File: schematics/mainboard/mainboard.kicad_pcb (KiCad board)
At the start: 2 copper layers, 166.4 x 91.4 mm, 31 parts, among them J1 ICSP, J2 USB_B_Micro, J3 DEALON DC-S050-200, J4 PWR_SELECT, J5 JOY1, J6 JOY2, J7 Throttle, U1 ATmega2560-16A, U2 FT232RL, U3 USBLC6-2P6, U4 AIP78M05, U5 L9110, Y1 16Mhz

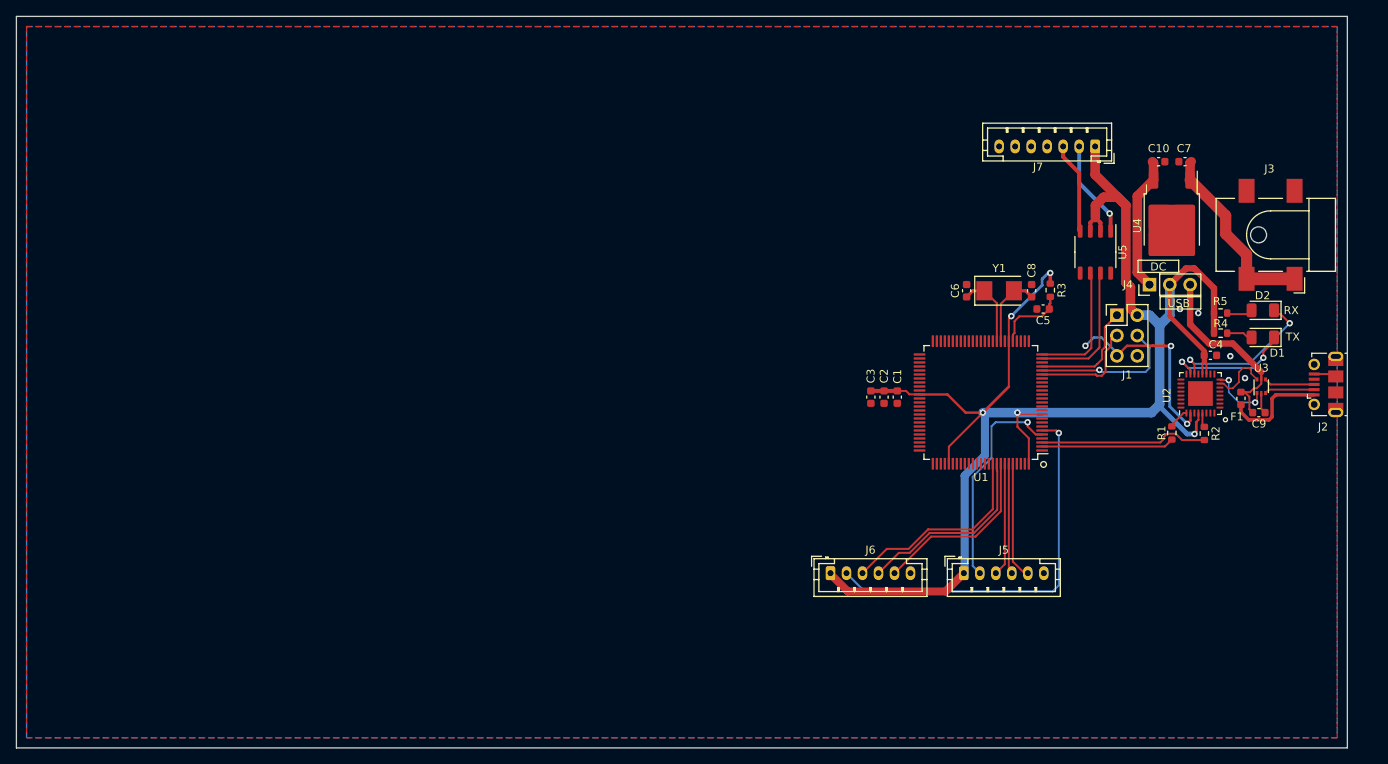
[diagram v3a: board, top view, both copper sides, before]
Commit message: SCH: mainboard=> DGAUGES header
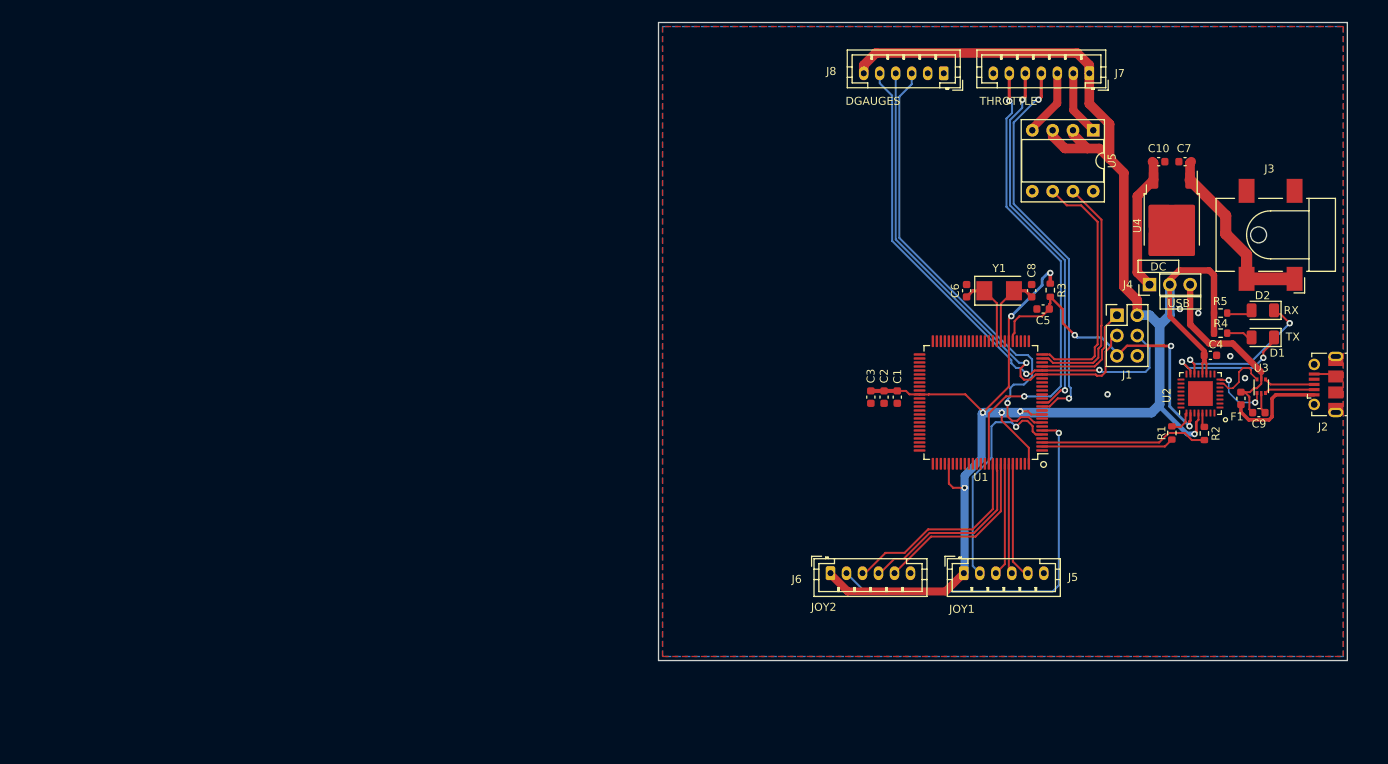
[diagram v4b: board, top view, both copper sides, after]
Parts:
- added J8: DGAUGES, Connector_JST:JST_PH_B6B-PH-K_1x06_P2.00mm_Vertical, F.Cu at (154.0, 28.7)
- U5: footprint Package_SO:SOP-8_3.9x4.9mm_P1.27mm -> Package_DIP:DIP-8_W7.62mm_Socket
- moved U5 15.2 mm to (172.7, 35.8)
- moved J7 9.17 mm to (172.2, 28.7)
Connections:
- U1 pad 8: unconnected-(U1-PE6-Pad8) -> Net-(J8-Pin_3)
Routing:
- net Net-(J7-Pin_6): track 0.00 -> 59.1 mm, vias 0 -> 2
- net Net-(J8-Pin_3): track 0.00 -> 58.3 mm, vias 0 -> 1
- net Net-(J7-Pin_4): track 0.00 -> 49.0 mm, vias 0 -> 2
- net /SCK: track 13.8 -> 62.4 mm, vias 0 -> 1
- net /MOSI: track 18.4 -> 66.1 mm, vias 1 -> 2
- net Net-(J7-Pin_5): track 0.00 -> 46.7 mm, vias 0 -> 2
- net +5V: track 207.2 -> 248.0 mm, vias 5 -> 7
- net /THROTTLE_DOWN: track 15.9 -> 31.1 mm
- net /THROTTLE_UP: track 17.1 -> 30.0 mm
- net /RESET: track 34.2 -> 41.9 mm
- net Net-(J7-Pin_2): track 12.2 -> 8.16 mm, vias 1 -> 0
- net Net-(J7-Pin_3): track 11.5 -> 8.42 mm
- net Net-(U2-TXD): track 2.43 -> 3.24 mm
- net Net-(J5-Pin_2): track 27.2 -> 27.9 mm
- net GND: vias 4 -> 5
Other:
- board size 166.4 x 91.4 mm -> 86.1 x 79.8 mm
- board text added: "DGAUGES"
- board text added: "JOY1"
- board text added: "JOY2"
- board text added: "THROTTLE"

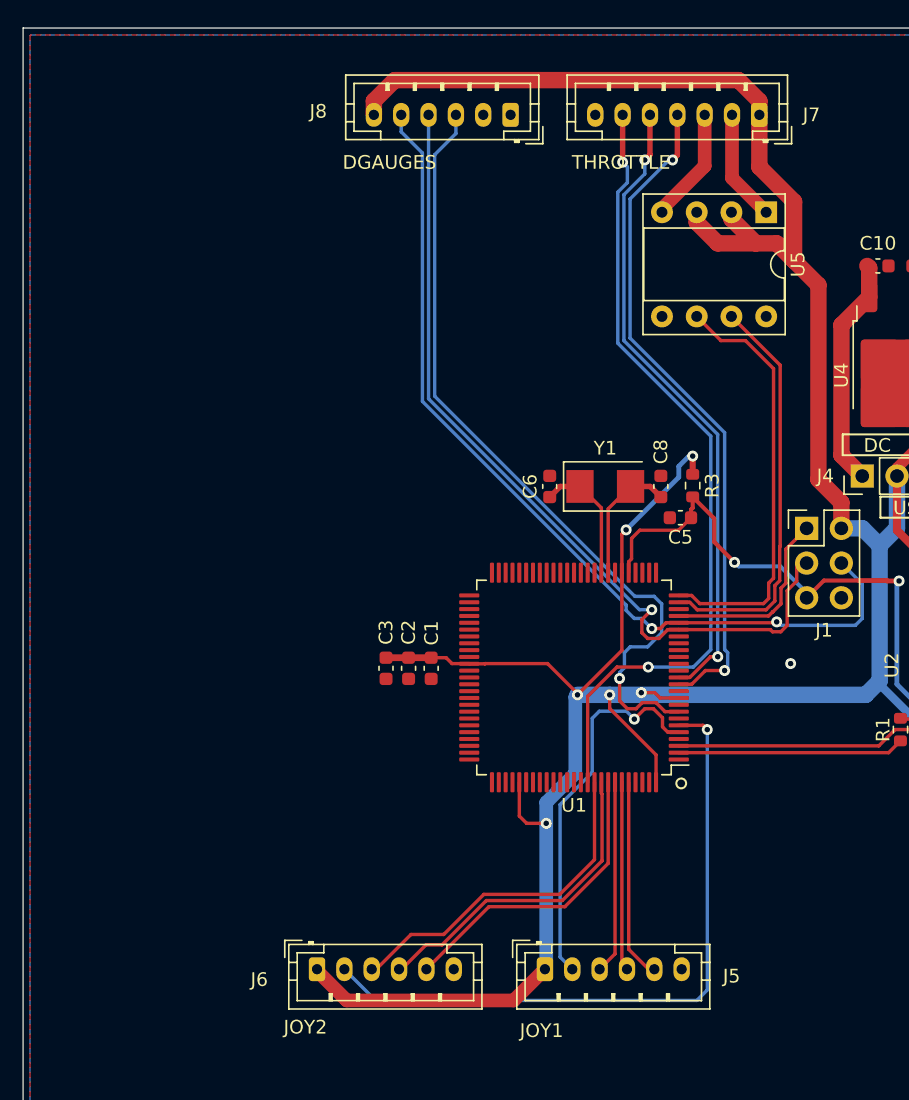
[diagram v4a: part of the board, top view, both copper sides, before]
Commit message: Mainboard: tweak pins, routed lcd connector
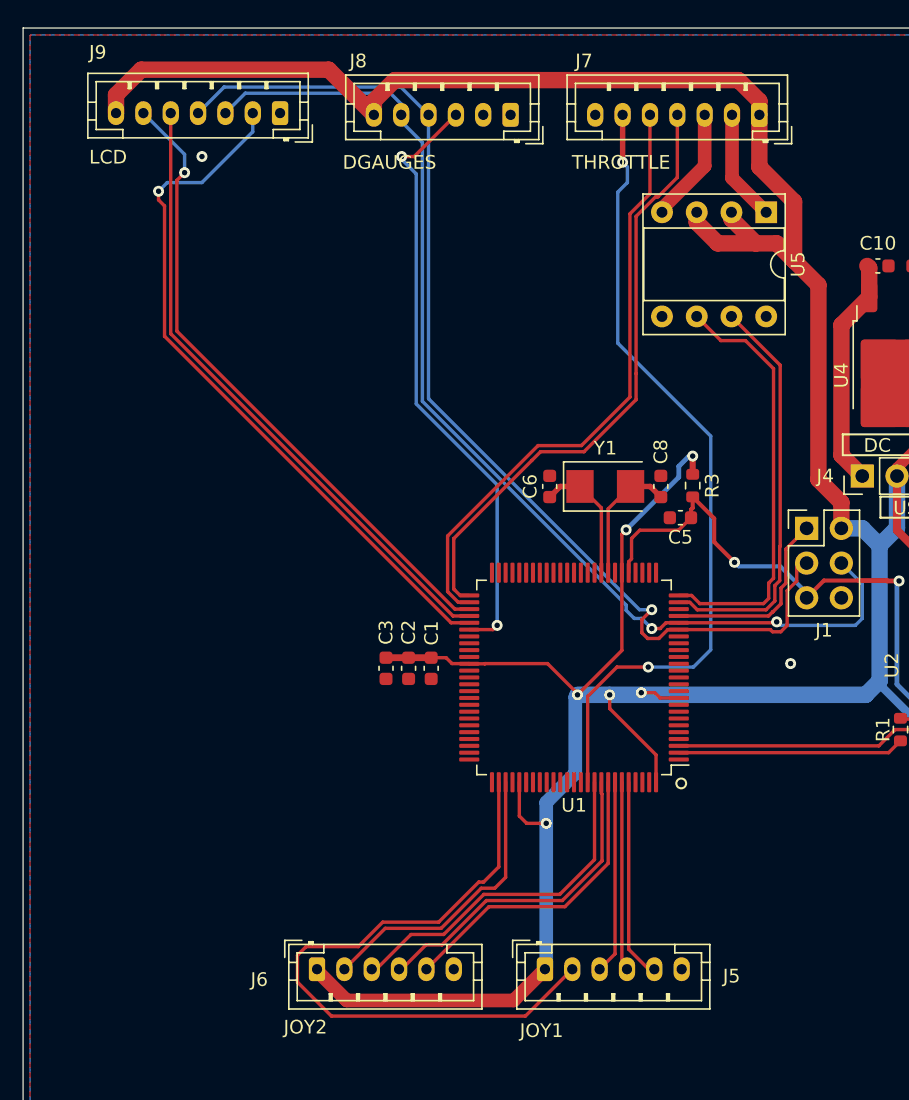
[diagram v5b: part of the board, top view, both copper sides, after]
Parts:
- added J9: LCD, Connector_JST:JST_PH_B7B-PH-K_1x07_P2.00mm_Vertical, F.Cu at (137.2, 28.6)
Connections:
- J5 pad 2: Net-(J5-Pin_2) -> /JOY1_PB
- J6 pad 2: Net-(J6-Pin_2) -> /JOY2_PB
- J8 pad 3: Net-(J8-Pin_3) -> /DG_LATCH
- U1 pad 12: Net-(J7-Pin_4) -> unconnected-(U1-PH0-Pad12)
- U1 pad 13: Net-(J7-Pin_5) -> unconnected-(U1-PH1-Pad13)
- U1 pad 5: Net-(J5-Pin_2) -> unconnected-(U1-PE3-Pad5)
- U1 pad 51: unconnected-(U1-PG0-Pad51) -> Net-(J7-Pin_4)
- U1 pad 52: unconnected-(U1-PG1-Pad52) -> Net-(J7-Pin_5)
- U1 pad 53: unconnected-(U1-PC0-Pad53) -> Net-(J9-Pin_6)
- U1 pad 54: unconnected-(U1-PC1-Pad54) -> Net-(J9-Pin_5)
- U1 pad 55: unconnected-(U1-PC2-Pad55) -> Net-(J9-Pin_2)
- U1 pad 56: unconnected-(U1-PC3-Pad56) -> /DG_LATCH
- U1 pad 6: Net-(J6-Pin_2) -> unconnected-(U1-PE4-Pad6)
- U1 pad 77: unconnected-(U1-PA1-Pad77) -> /JOY1_PB
- U1 pad 78: unconnected-(U1-PA0-Pad78) -> /JOY2_PB
- U1 pad 8: Net-(J8-Pin_3) -> unconnected-(U1-PE6-Pad8)
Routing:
- net Net-(J8-Pin_3): track 58.3 -> 0.00 mm, vias 1 -> 0
- net Net-(J9-Pin_2): track 0.00 -> 51.8 mm, vias 0 -> 1
- net Net-(J6-Pin_2): track 49.1 -> 0.00 mm, vias 1 -> 0
- net /JOY1_PB: track 0.00 -> 48.1 mm
- net Net-(J9-Pin_6): track 0.00 -> 47.2 mm, vias 0 -> 1
- net Net-(J9-Pin_5): track 0.00 -> 46.5 mm
- net /DG_LATCH: track 0.00 -> 44.6 mm, vias 0 -> 2
- net Net-(J5-Pin_2): track 27.9 -> 0.00 mm, vias 1 -> 0
- net +5V: track 248.0 -> 270.4 mm
- net /JOY2_PB: track 0.00 -> 21.5 mm
- net /SCK: track 62.4 -> 80.8 mm
- net /MOSI: track 66.1 -> 80.7 mm
- net Net-(J7-Pin_4): track 49.0 -> 44.7 mm, vias 2 -> 0
- net Net-(J7-Pin_5): track 46.7 -> 44.8 mm, vias 2 -> 0
- net GND: vias 5 -> 6
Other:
- board text added: "LCD"

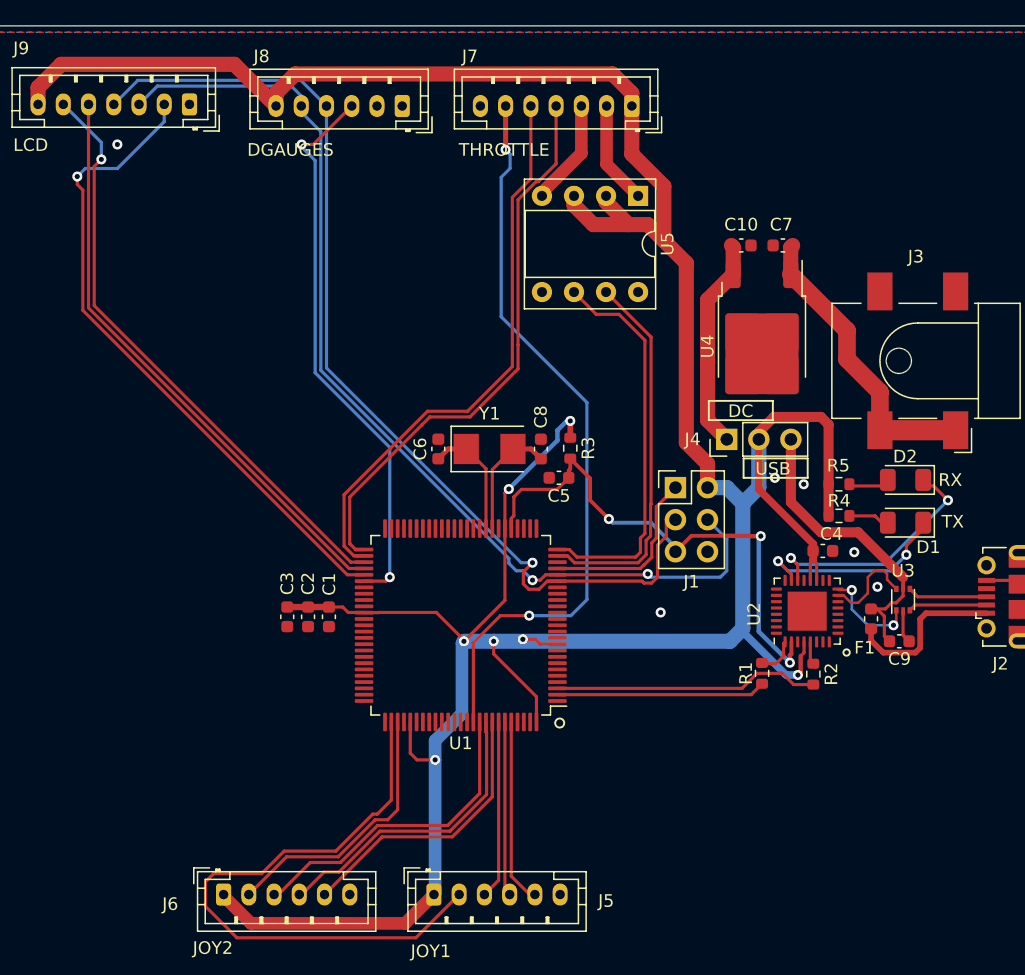
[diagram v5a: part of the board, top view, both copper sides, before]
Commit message: SCH: mainboard missing cap & gnd connections on ft232
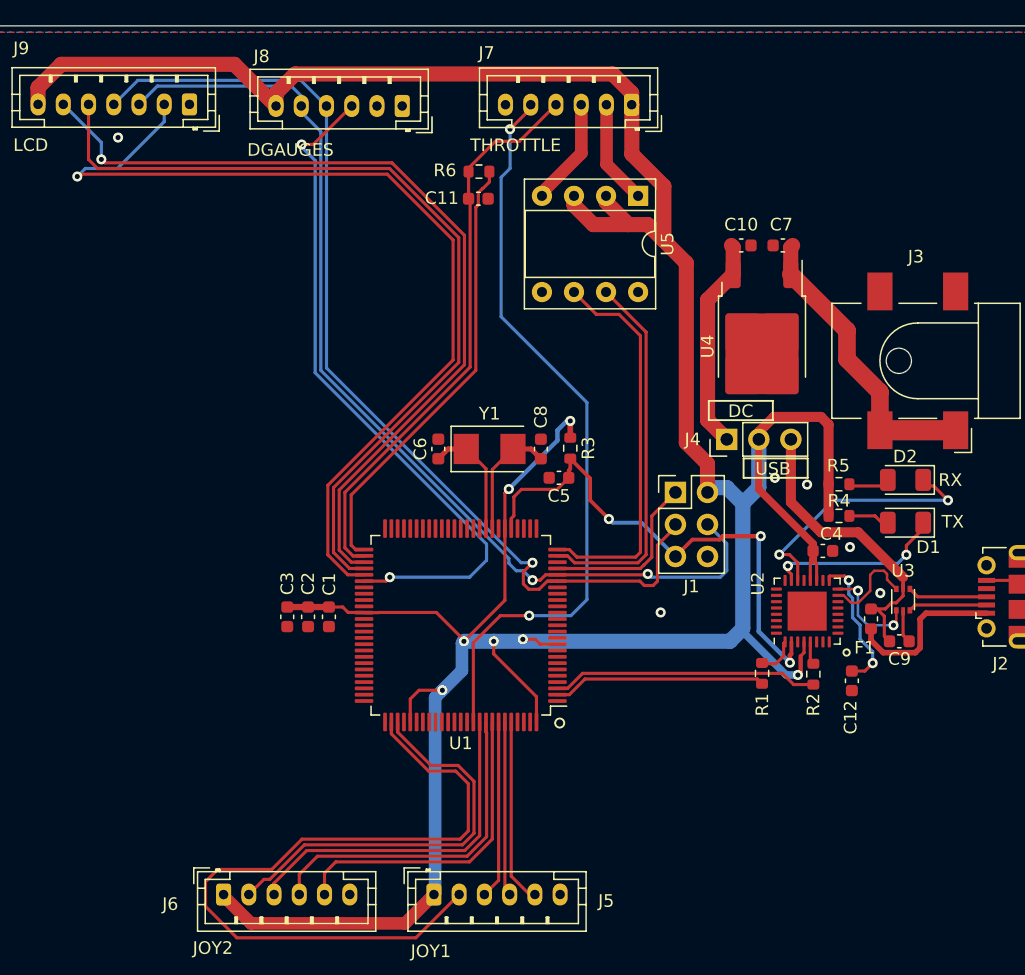
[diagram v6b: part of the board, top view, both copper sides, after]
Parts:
- added C11: 50pF, Capacitor_SMD:C_0603_1608Metric, F.Cu at (160.1, 36.0)
- added C12: 100nF, Capacitor_SMD:C_0603_1608Metric, F.Cu at (189.7, 74.2)
- added R6: 1M, Resistor_SMD:R_0603_1608Metric, F.Cu at (160.1, 33.9)
- J7: value Throttle -> Conn_01x06_Pin; footprint Connector_JST:JST_PH_B7B-PH-K_1x07_P2.00mm_Vertical -> Connector_JST:JST_PH_B6B-PH-K_1x06_P2.00mm_Vertical
- moved J1 0.38 mm to (175.7, 59.3)
- moved J7 0.10 mm to (172.2, 28.6)
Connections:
- J7 pad 4: Net-(J7-Pin_4) -> /THROTTLE_TOUCH
- J7 pad 5: Net-(J7-Pin_5) -> /THROTTLE_POT
- J7 pad 6: Net-(J7-Pin_6) -> GND
- U1 pad 51: Net-(J7-Pin_4) -> Net-(U1-PG0)
- U1 pad 52: Net-(J7-Pin_5) -> /THROTTLE_TOUCH
- U1 pad 90: Net-(J7-Pin_6) -> /THROTTLE_POT
- U2 pad 17: unconnected-(U2-3V3OUT-Pad17) -> Net-(U2-3V3OUT)
- U2 pad 26: unconnected-(U2-TEST-Pad26) -> GND
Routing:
- net /THROTTLE_POT: track 0.00 -> 59.7 mm, vias 0 -> 2
- net Net-(J7-Pin_6): track 59.1 -> 0.00 mm, vias 2 -> 0
- net /THROTTLE_TOUCH: track 0.00 -> 45.0 mm
- net Net-(J7-Pin_5): track 44.8 -> 0.00 mm
- net Net-(J7-Pin_4): track 44.7 -> 0.00 mm
- net Net-(U1-PG0): track 0.00 -> 35.3 mm
- net Net-(J9-Pin_2): track 51.8 -> 74.7 mm
- net Net-(J9-Pin_5): track 46.5 -> 68.3 mm
- net Net-(J9-Pin_6): track 47.2 -> 68.3 mm
- net /JOY1_PB: track 48.1 -> 59.4 mm
- net Net-(U2-3V3OUT): track 0.00 -> 11.3 mm, vias 0 -> 2
- net /JOY2_PB: track 21.5 -> 32.4 mm
- net /DG_LATCH: track 44.6 -> 54.6 mm
- net Net-(J6-Pin_5): track 22.4 -> 25.4 mm
- net Net-(J6-Pin_4): track 23.9 -> 26.8 mm
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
